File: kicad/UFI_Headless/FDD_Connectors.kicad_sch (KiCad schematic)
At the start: 16 parts, among them J6 FDD_34PIN, J7 AMIGA_FDD, Q12 BSS138DW

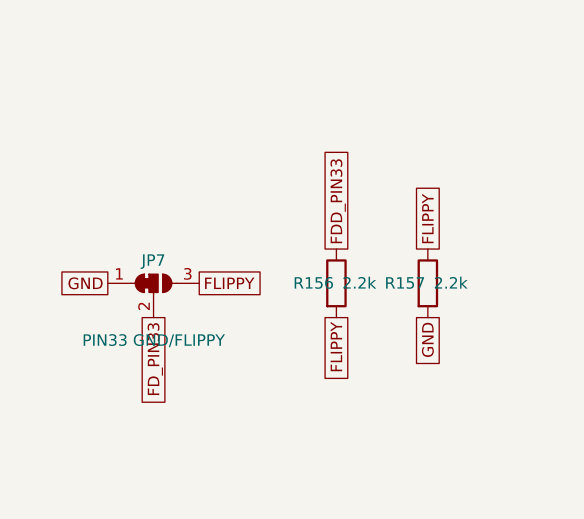
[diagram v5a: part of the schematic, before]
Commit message: KiCad v0.7 rework, stage A11f (fixes from the A8 review, owner decisions of 2026-10-25): F1 - the write gate is now hard-gated by a NOR instead of the A11a OR that had driven the MOSFET gate the wrong way since A11b: new U31 74LVC1G02 (MDD 74LVC1G02GW C52953351, SOT-353) on Flux_Interface forms Q9 gate = NOR(WGATE_n, LOCK), PE14 becomes WGATE_n (active low on every board revision again) with R167 10k pull-up to +3V3 so reset and boot leave the gate released, C88 100 nF; U30 gate 1 retired (1A/1B on GND, 1Y no-connect), gate 2 still gates APL_WRREQ with LOCK; netlist: FDD_WGATE = U5.67 R167 U31.1 J21.7, FDD_WGATE_G = U31.4 Q9.2 R151 TP8, LOCK = U14.4 U30.6 U31.2. Firmware in the same commit: board.h bus_out_inverted() excludes PE14, board_headless.c latches PE14 high at start-up; truth table for every MOSFET-driven line (reset / idle / active) recorded in PLAN.md, measurement point "J6 pin 24 stays high with the lock set during a read" in the README row, self-test item planned for A10; protocol doc (one hunk in the board_status bit 0 note). R1: D30 removed, SYNC_5V protected by the 5 V channel IO3 of D31 ESDA6V1-5SC6, J19 becomes a keyed JST B3B-XH-A (C144394). R2: J20 GUARD becomes JST B4B-XH-A (C144395) with D32-D34 PESD3V3L1BA (C51450) on GUARD_OFF_J/ERR5_J/ERR12_J; note that the Guard board v0.2 gets a JST XH J3 too. R3: flippy divider kept at 2.4k/2.4k (C22940, Greaseweazle V4.1 compatible), JP7 default GND. ERC over the whole project 0 errors / 0 warnings (build/erc.rpt). ARM build 0 warnings; offline gate as reported in the stage log. PLAN.md (A11f, polarity table), kicad README (A11f row). PCB follows in B3.
Claude-Session: https://claude.ai/code/session_014MdzrcyXuayppPHbfEjUrw
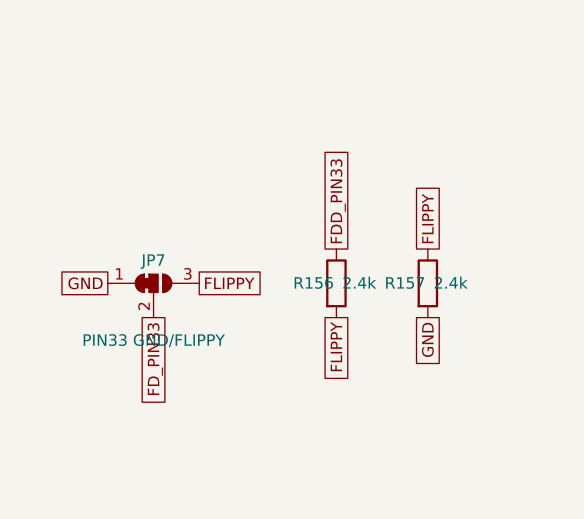
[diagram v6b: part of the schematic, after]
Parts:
- R156: value 2.2k -> 2.4k; LCSC C4190 -> C22940; MPN (none) -> 2.4k (flippy divider, Greaseweazle V4.1 compatible; owner 2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
- R157: value 2.2k -> 2.4k; LCSC C4190 -> C22940
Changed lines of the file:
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@@
 			)
 		)
-		(property "Value" "2.2k"
+		(property "Value" "2.4k"
 			(at 262.89 299.72 0)
 			(show_name no)
@@
 			)
 		)
-    (property "LCSC" "C4190" (at 260.35 299.72 0)
+    (property "LCSC" "C22940" (at 260.35 299.72 0)
+      (effects (font (size 1.27 1.27)) (hide yes))
+    )
+    (property "MPN" "2.4k (flippy divider, Greaseweazle V4.1 compatible; owner 25.10.)" (at 260.35 299.72 0)
       (effects (font (size 1.27 1.27)) (hide yes))
     )
@@
 			)
 		)
-		(property "Value" "2.2k"
+		(property "Value" "2.4k"
 			(at 273.05 299.72 0)
 			(show_name no)
@@
 			)
 		)
-    (property "LCSC" "C4190" (at 270.51 299.72 0)
+    (property "LCSC" "C22940" (at 270.51 299.72 0)
       (effects (font (size 1.27 1.27)) (hide yes))
     )

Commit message: KiCad v0.7 rework, stage C part 1 (BOM completion before the release, review note H12): every BOM row now carries an LCSC number, checked against the JLCPCB SMT catalogue on 2026-10-25 (stock in brackets). LAN sheet: U23 W5500 C32843 (9019), J22 HR911105A C12074 (72229, THT), Y2 25 MHz 12 pF +-10 ppm YXC X322525MOB4SI C9006 (basic; load capacitance 12 pF verified on the LCSC parameter page, fits the 18 pF C59/C60), C59/C60 18 pF C0G Yageo CC0603JRNPO9BN180 C107040, C61/C74 10 nF FH 0603B103K500NT C57112 (basic), C71 22 nF Samsung CL10B223KB8NNNC C21122 (basic), C72/C73 6.8 nF FH 0603B682K500NT C1631 (basic), C62 4.7 uF C1779, C63/C69 10 uF C15850, C64-C68/C70 100 nF C14663, FB2 C1002, R109 1M C22935, R111 12.4k 1 % C22865, R112/R113 49.9R 1 % C23185 (basic), R114 10R 1 % C22859 (basic), R115/R116 82R 1 % C23255, R117/R118 330R C23138, R119-R124 10k C25804. Other sheets: R75-R99/R105/R128 1k C21190, R74/R107/R108 10k C25804, R101-R104/R130 470R C23179, R106/R131 100k C25803, C58 100 nF C14663 (value text 100n -> 100nF so it groups with the other 100 nF), D18-D26/D28/D29 PESD3V3L1BA C51450 (48710) like D32-D34, Q5 2N7002 C8545 (basic), U22 TS5A3166DBVR C353035 (10678), J2 DC-005 2.0 C16214 (92305; same pin pattern as the KiCad BarrelJack_Horizontal footprint, placement to be checked in the JLC viewer), J7 2x12 IDC ZHOURI DC3-2.54-24PAS C5144580 (stock 81 - hand soldering stays the recommendation in docs/Bestellung_JLC.md), J12 2x8 IDC DC3-2.54-16PAS C2977594 (4335), J16 2x5 pin header XFCN PZ254V-12-10P C492422 (105667), J21 2x10 pin header PZ254V-12-20P C492427 (63622). Solder jumpers JP5-JP8 are excluded from the BOM (in_bom no) like JP1/JP3 - bare copper, nothing to place. Stock of the review's watch list: U9 SN74LS07DR C371970 4776, D31 ESDA6V1-5SC6 C6650 3010, L1 SRN6045TA-150M C1330797 1866. BOM export (kicad-cli sch export bom, grouped by value/footprint/LCSC): 99 rows, 0 without LCSC, 0 DNP. ERC over the whole project 0 errors / 0 warnings (build/erc.rpt). No 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
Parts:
- J7: LCSC (none) -> C5144580
- JP7: now left out of the parts list
- R97, R98, R99: LCSC (none) -> C21190
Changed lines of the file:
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@@
+			)
+		)
+		(property "LCSC" "C5144580"
+			(at 259.08 109.22 0)
+			(effects
+				(font
+					(size 1.27 1.27)
+				)
+				(hide yes)
 			)
 		)
@@
 			)
 		)
+		(property "LCSC" "C21190"
+			(at 252.222 201.93 90)
+			(effects
+				(font
+					(size 1.27 1.27)
+				)
+				(hide yes)
+			)
+		)
 		(property "Footprint" "Resistor_SMD:R_0603_1608Metric"
 			(at 252.222 201.93 90)
@@
 			)
 		)
+		(property "LCSC" "C21190"
+			(at 254.762 201.93 90)
+			(effects
+				(font
+					(size 1.27 1.27)
+				)
+				(hide yes)
+			)
+		)
 		(property "Footprint" "Resistor_SMD:R_0603_1608Metric"
 			(at 254.762 201.93 90)
@@
 					(size 1.27 1.27)
 				)
+			)
+		)
+		(property "LCSC" "C21190"
+			(at 257.302 201.93 90)
+			(effects
+				(font
+					(size 1.27 1.27)
+				)
+				(hide yes)
 			)
 		)
@@
 		(unit 1)
 		(exclude_from_sim no)
-		(in_bom yes)
-		(on_board yes)
-		(dnp no)
+		(in_bom no)
+		(on_board yes)
+		(dnp no)
